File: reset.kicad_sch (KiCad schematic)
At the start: 4 parts, among them U10 LM2901

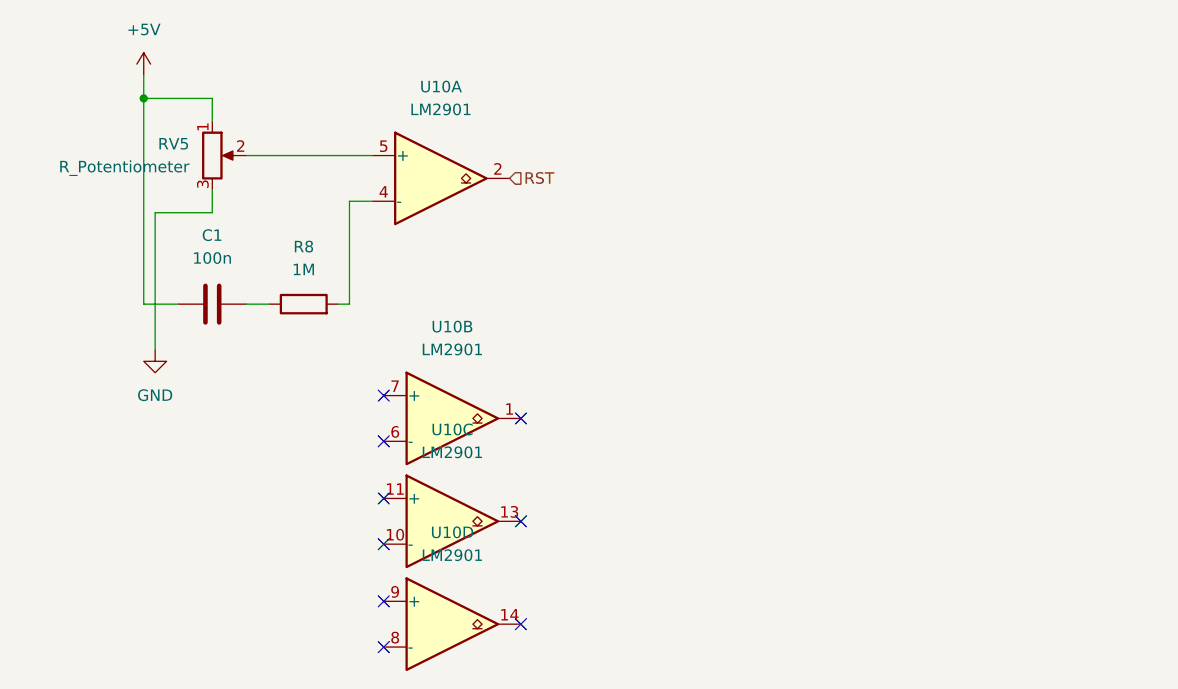
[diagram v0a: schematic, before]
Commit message: Switch reset driver to MAX6895
Signed-off-by: Oliver Gaskell <og305@cam.ac.uk>
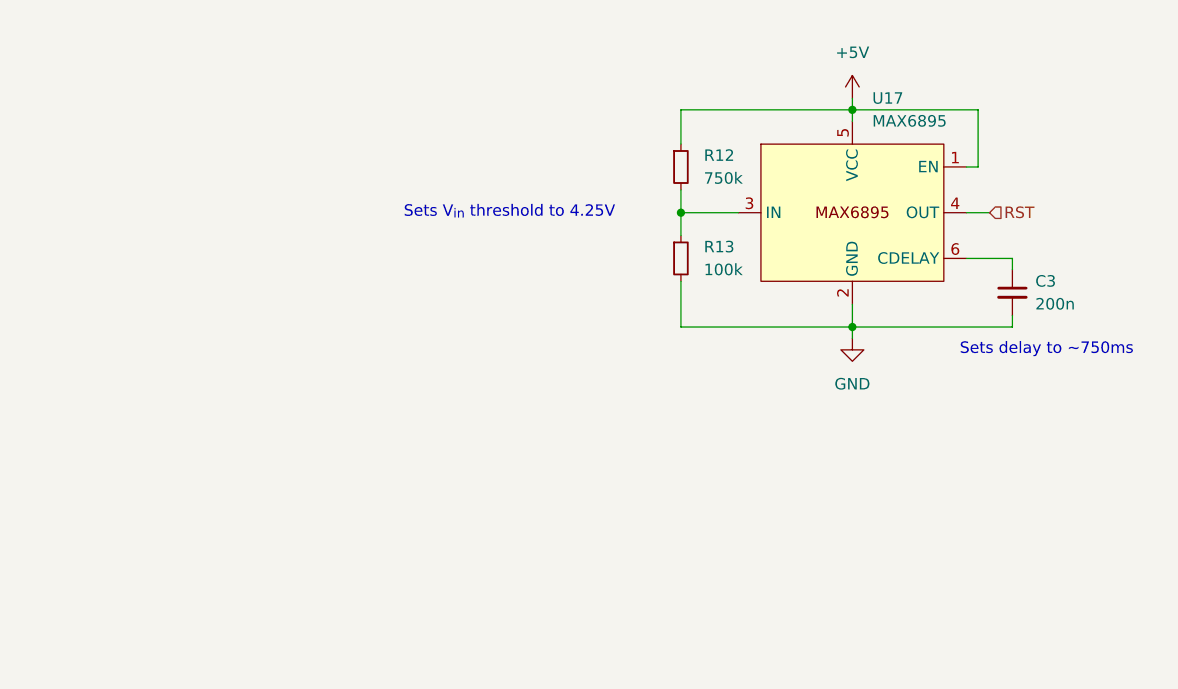
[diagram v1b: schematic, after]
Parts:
- removed C1: 100n, Capacitor_THT:C_Disc_D5.0mm_W2.5mm_P5.00mm, symbol Device:C
- removed R8: 1M, Resistor_THT:R_Axial_DIN0207_L6.3mm_D2.5mm_P7.62mm_Horizontal, symbol Device:R
- removed RV5: R_Potentiometer, Potentiometer_THT:Potentiometer_Bourns_3296Y_Vertical, symbol Device:R_Potentiometer
- removed U10: LM2901, Package_DIP:DIP-14_W7.62mm_Socket, symbol Comparator:LM2901
- added C3: 200n, symbol Device:C_Small
- added R12: 750k, symbol Device:R_Small
- added R13: 100k, symbol Device:R_Small
- added U17: MAX6895, Package_TO_SOT_SMD:SOT-23-6_Handsoldering, symbol FBR_Symbols:MAX6895
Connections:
- net +5V: now also R12.1, U17.1 (EN), U17.5 (VCC)
- net GND: now also C3.2, R13.2, U17.2 (GND)
- net RST: now also U17.4 (OUT)
- new net: R12.2, R13.1, U17.3 (IN)
- new net: C3.1, U17.6 (CDELAY)
- no-connect marks 9 -> 0
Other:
- note added: "Sets V_{in} threshold to 4.25V"
- note added: "Sets delay to ~750ms"

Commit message: Complete new version
Signed-off-by: Oliver Gaskell <og305@cam.ac.uk>
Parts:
- C3: footprint (none) -> Capacitor_SMD:C_0603_1608Metric_Pad1.08x0.95mm_HandSolder
- R12, R13: footprint (none) -> Resistor_SMD:R_0603_1608Metric_Pad0.98x0.95mm_HandSolder
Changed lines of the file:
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@@
 			)
 		)
-		(property "Footprint" ""
+		(property "Footprint" "Resistor_SMD:R_0603_1608Metric_Pad0.98x0.95mm_HandSolder"
 			(at 165.1 59.69 0)
 			(effects
@@
 			)
 		)
-		(property "Footprint" ""
+		(property "Footprint" "Capacitor_SMD:C_0603_1608Metric_Pad1.08x0.95mm_HandSolder"
 			(at 201.93 63.5 0)
 			(effects
@@
 			)
 		)
-		(property "Footprint" ""
+		(property "Footprint" "Resistor_SMD:R_0603_1608Metric_Pad0.98x0.95mm_HandSolder"
 			(at 165.1 49.53 0)
 			(effects
